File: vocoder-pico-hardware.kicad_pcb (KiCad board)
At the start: 2 copper layers, 47 x 108 mm, 68 parts, among them J1 Conn_02x05_Odd_Even, J2 AudioJack2_SwitchT, J3 AudioJack2_SwitchT, Q1 BC547, Q2 BC547, Q3 BC547, Q4 BC547, SW1 SW_Push, SW2 SW_Push, U1 TL072, U2 LM7805_TO220, U3 PCM5100A, U4 SC39-11GWA, U5 SC39-11GWA, U6 SC39-11GWA, U7 SC39-11GWA, U8 MCP6002-xP

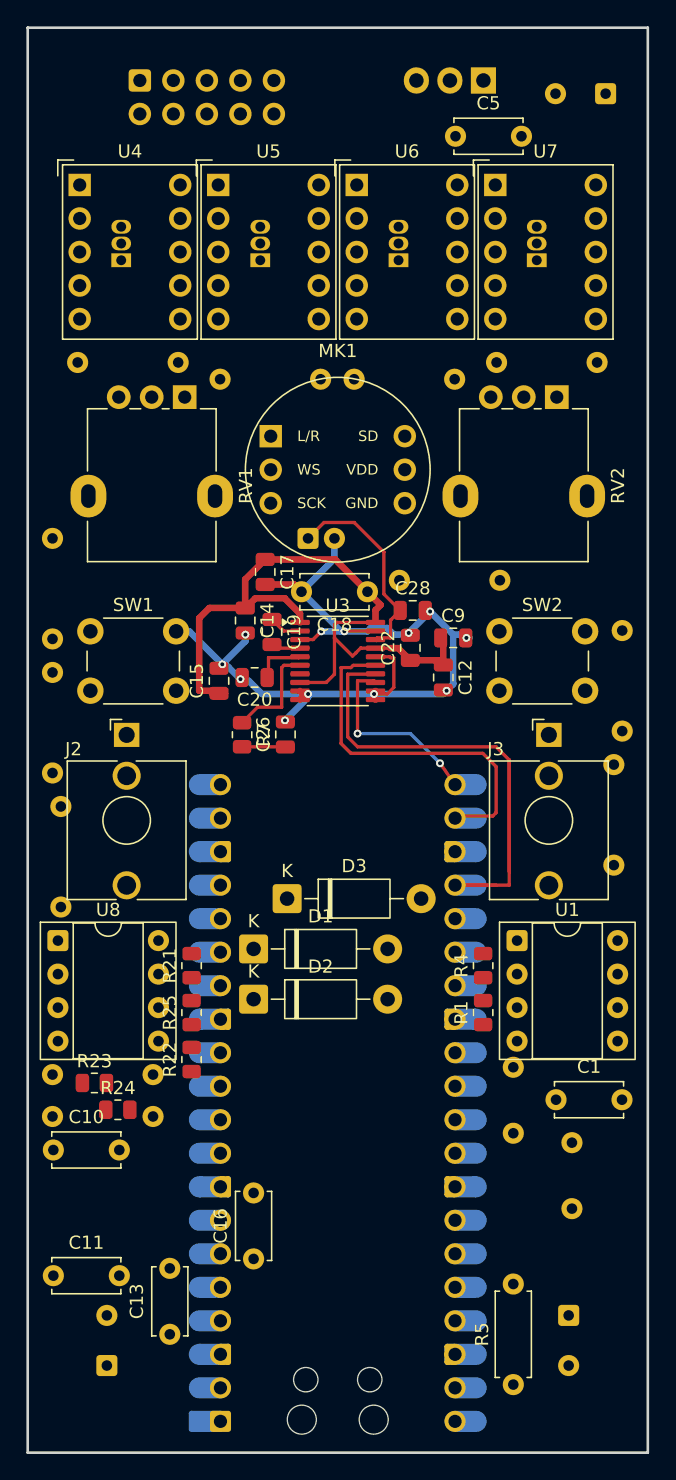
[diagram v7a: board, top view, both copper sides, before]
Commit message: begin routing of inmp441 i2s section
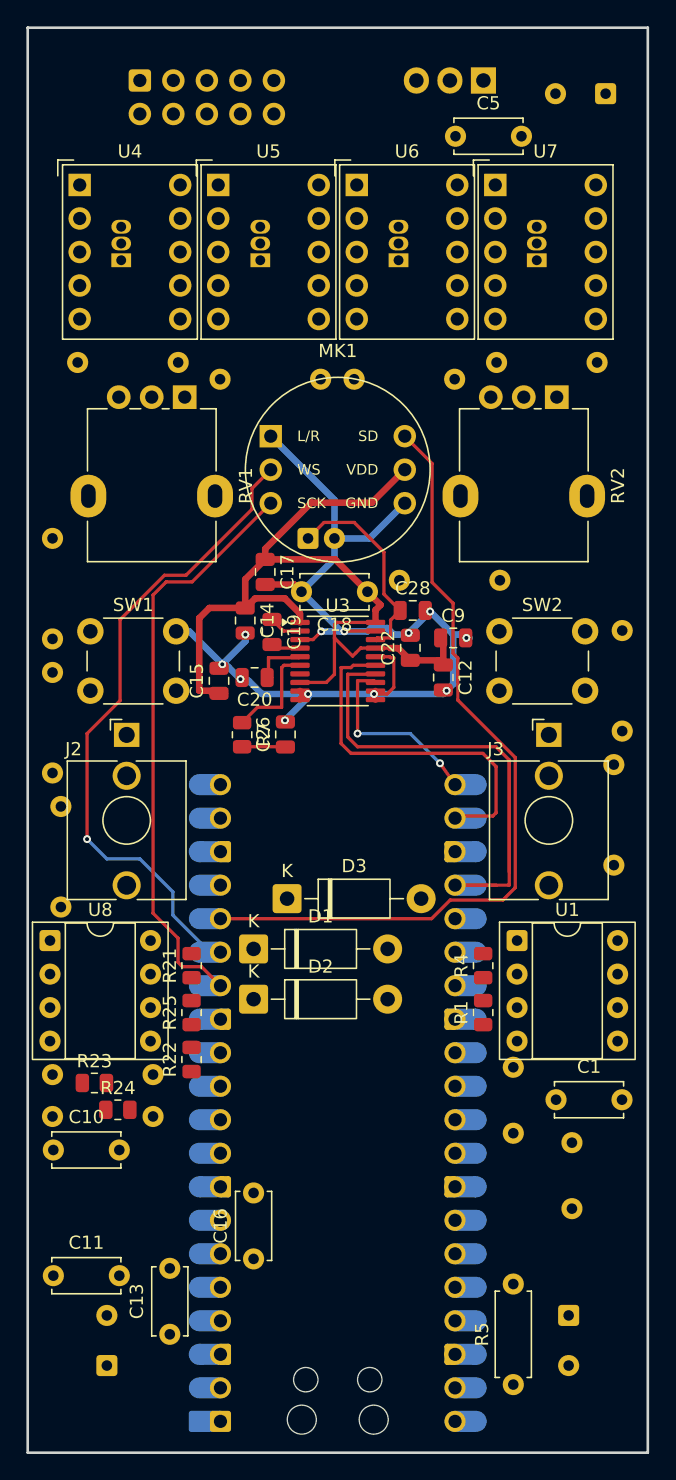
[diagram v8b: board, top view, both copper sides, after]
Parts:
- moved U8 0.60 mm to (55.7, 99.2)
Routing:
- net Net-(A1-GPIO12): track 0.80 -> 61.8 mm
- net Net-(A1-GPIO11): track 0.00 -> 49.0 mm, vias 0 -> 1
- net Net-(A1-GPIO10): track 0.00 -> 44.4 mm
- net GND: track 70.7 -> 86.9 mm
- net Vdd: track 55.1 -> 68.9 mm
